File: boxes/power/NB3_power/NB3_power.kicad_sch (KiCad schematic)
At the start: 82 parts, among them J1 Barrel_Jack_PJ-036AH-SMT-TR, J2 Conn_01x02_Male, J3 Conn_01x02_Male, J4 Conn_01x02_Male, J5 Conn_01x04_Male, J6 Conn_01x02_Male, J7 Conn_01x02_Male, Q1 PMOS, Q2 NMOS, SW1 SW_SPDT, U1 NiMH_Charger_LTC4010, U2 Voltage_Regulator_AP64501

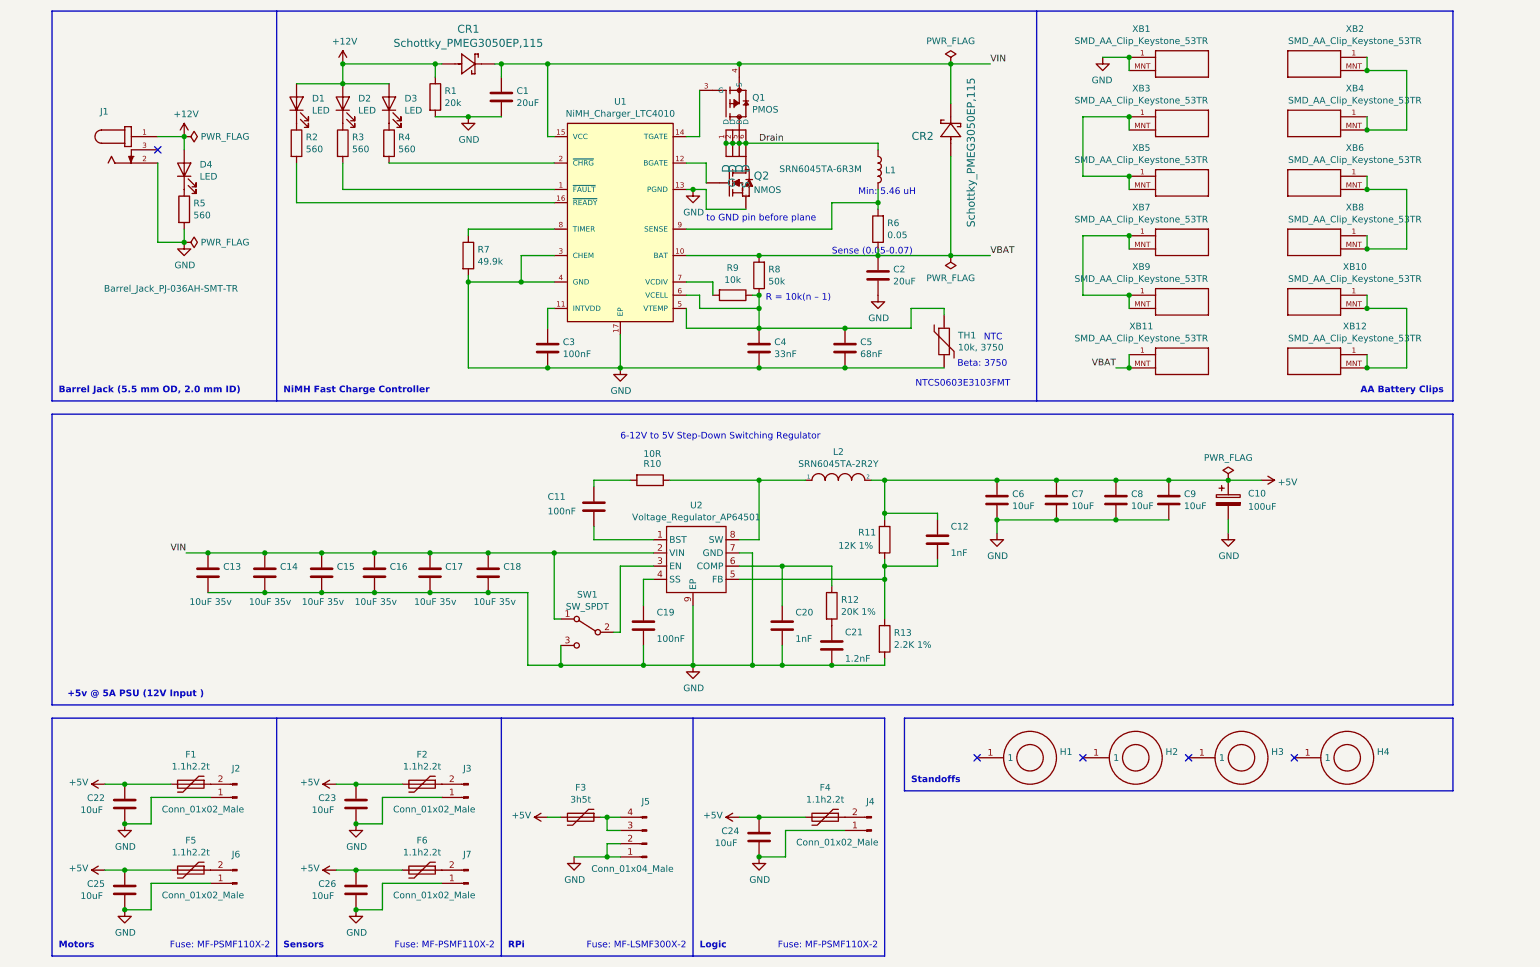
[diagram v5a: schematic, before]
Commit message: NB3_power PCB layout finished
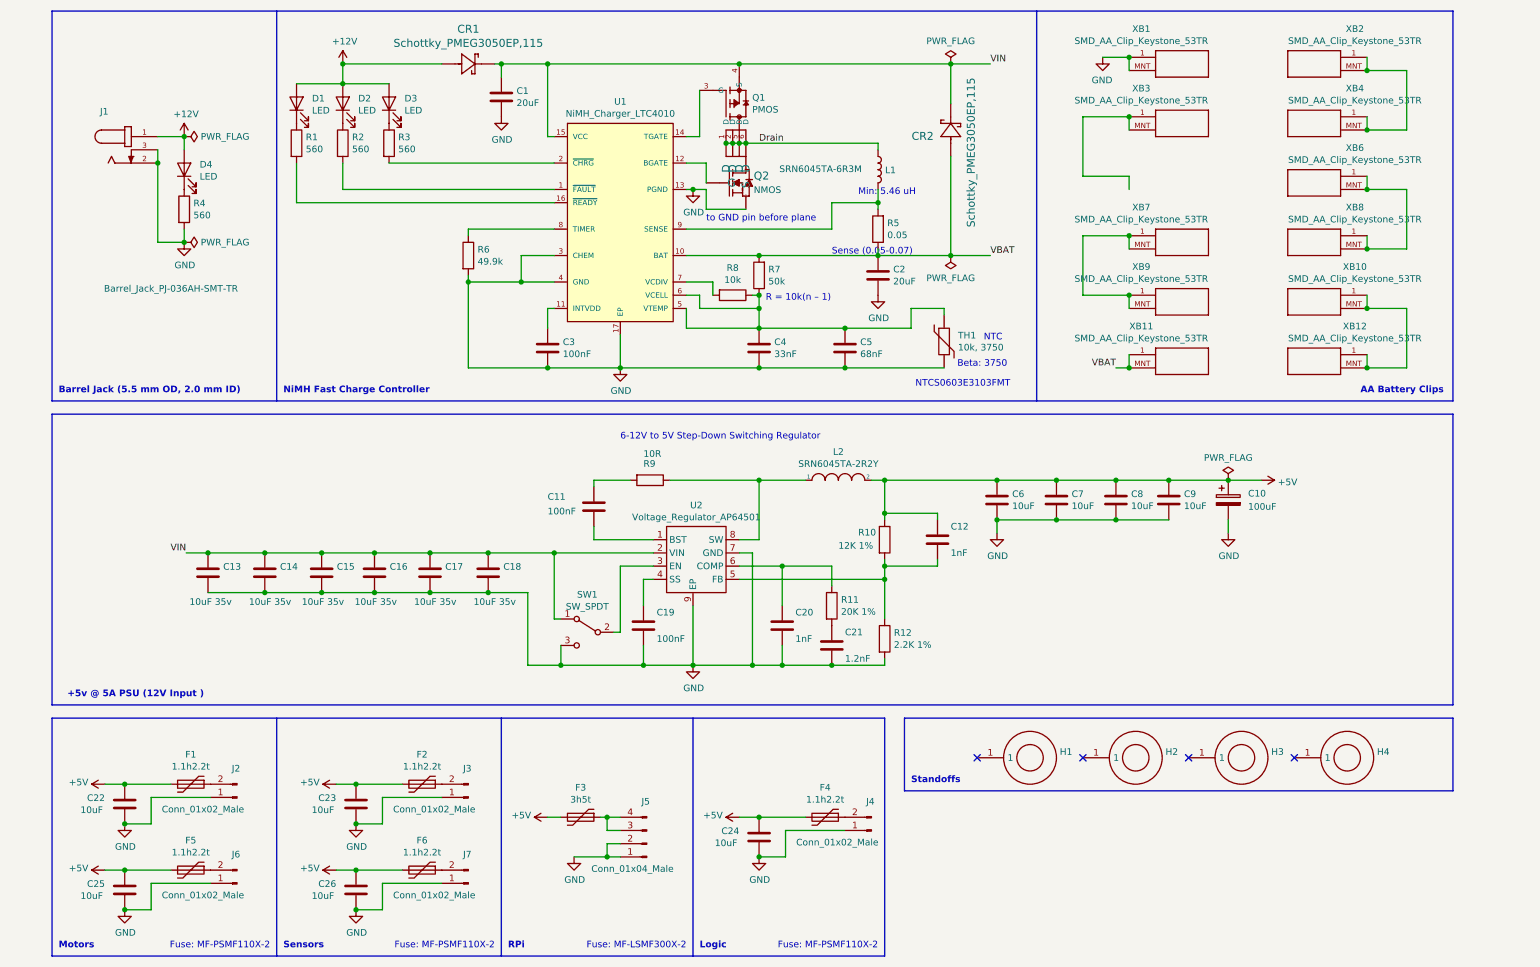
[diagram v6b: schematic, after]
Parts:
- removed R1: 20k, Resistor_SMD:R_0402_1005Metric, symbol Device:R
- removed XB5: SMD_AA_Clip_Keystone_53TR, NB3_power:SMD_AA_Clip_Keystone_53TR, symbol NB3_power:SMD_AA_Clip_Keystone_53TR
- F3: footprint Fuse:Fuse_Bourns_MF-SM_7.98x5.44mm -> Fuse:Fuse_2920_7451Metric
- renumbered R2 to R1, R11 to R10, R12 to R11, R13 to R12, R3 to R2, R4 to R3, R5 to R4, R6 to R5, R7 to R6, R8 to R7, R9 to R8, R10 to R9
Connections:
- net GND: now also J1.3
- no-connect marks 5 -> 4

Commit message: NB3_power PCB fab submisson
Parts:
- C1, C2: value 20uF -> 22uF
- R1, R2, R3, R4: value 560 -> 5.6k
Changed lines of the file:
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@@
   (junction (at 266.7 71.12) (diameter 1.016) (color 0 0 0 0))
   (junction (at 266.7 82.55) (diameter 1.016) (color 0 0 0 0))
-  (no_connect (at 252.73 157.48))
   (no_connect (at 212.09 157.48))
-  (no_connect (at 191.77 157.48))
+  (no_connect (at 252.73 157.48))
   (no_connect (at 232.41 157.48))
+  (no_connect (at 191.77 157.48))
   (wire (pts (xy 24.13 162.56) (xy 27.94 162.56))
     (stroke (width 0) (type solid) (color 0 0 0 0))
@@
       (effects (font (size 1.27 1.27)) (justify left))
     )
-    (property "Value" "560" (id 1) (at 41.148 53.213 0)
+    (property "Value" "5.6k" (id 1) (at 41.148 53.213 0)
       (effects (font (size 1.27 1.27)) (justify left))
     )
@@
       (effects (font (size 1.27 1.27)) (justify left))
     )
-    (property "Value" "560" (id 1) (at 62.738 40.513 0)
+    (property "Value" "5.6k" (id 1) (at 62.738 40.513 0)
       (effects (font (size 1.27 1.27)) (justify left))
     )
@@
       (effects (font (size 1.27 1.27)) (justify left))
     )
-    (property "Value" "560" (id 1) (at 71.628 40.513 0)
+    (property "Value" "5.6k" (id 1) (at 71.628 40.513 0)
       (effects (font (size 1.27 1.27)) (justify left))
     )
@@
       (effects (font (size 1.27 1.27)) (justify left))
     )
-    (property "Value" "560" (id 1) (at 80.518 40.513 0)
+    (property "Value" "5.6k" (id 1) (at 80.518 40.513 0)
       (effects (font (size 1.27 1.27)) (justify left))
     )
@@
       (effects (font (size 1.27 1.27)) (justify left))
     )
-    (property "Value" "20uF" (id 1) (at 103.251 31.623 0)
+    (property "Value" "22uF" (id 1) (at 103.251 31.623 0)
       (effects (font (size 1.27 1.27)) (justify left))
     )
@@
       (effects (font (size 1.27 1.27)) (justify left))
     )
-    (property "Value" "20uF" (id 1) (at 175.641 65.913 0)
+    (property "Value" "22uF" (id 1) (at 175.641 65.913 0)
       (effects (font (size 1.27 1.27)) (justify left))
     )
@@
     )
     (path "/00000000-0000-0000-0000-00005f7de0af"
-      (reference "C1") (unit 1) (value "20uF") (footprint "Capacitor_SMD:C_0805_2012Metric")
+      (reference "C1") (unit 1) (value "22uF") (footprint "Capacitor_SMD:C_0805_2012Metric")
     )
     (path "/00000000-0000-0000-0000-00005f819ed1"
-      (reference "C2") (unit 1) (value "20uF") (footprint "Capacitor_SMD:C_0805_2012Metric")
+      (reference "C2") (unit 1) (value "22uF") (footprint "Capacitor_SMD:C_0805_2012Metric")
     )
     (path "/00000000-0000-0000-0000-00005f80414d"
@@
     )
     (path "/00000000-0000-0000-0000-00005f7ee2db"
-      (reference "R1") (unit 1) (value "560") (footprint "Resistor_SMD:R_0402_1005Metric")
+      (reference "R1") (unit 1) (value "5.6k") (footprint "Resistor_SMD:R_0402_1005Metric")
     )
     (path "/00000000-0000-0000-0000-00005f7eeac0"
-      (reference "R2") (unit 1) (value "560") (footprint "Resistor_SMD:R_0402_1005Metric")
+      (reference "R2") (unit 1) (value "5.6k") (footprint "Resistor_SMD:R_0402_1005Metric")
     )
     (path "/00000000-0000-0000-0000-00005f7ee754"
-      (reference "R3") (unit 1) (value "560") (footprint "Resistor_SMD:R_0402_1005Metric")
+      (reference "R3") (unit 1) (value "5.6k") (footprint "Resistor_SMD:R_0402_1005Metric")
     )
     (path "/00000000-0000-0000-0000-00005f8745a5"
-      (reference "R4") (unit 1) (value "560") (footprint "Resistor_SMD:R_0402_1005Metric")
+      (reference "R4") (unit 1) (value "5.6k") (footprint "Resistor_SMD:R_0402_1005Metric")
     )
     (path "/00000000-0000-0000-0000-00005f83ae1a"

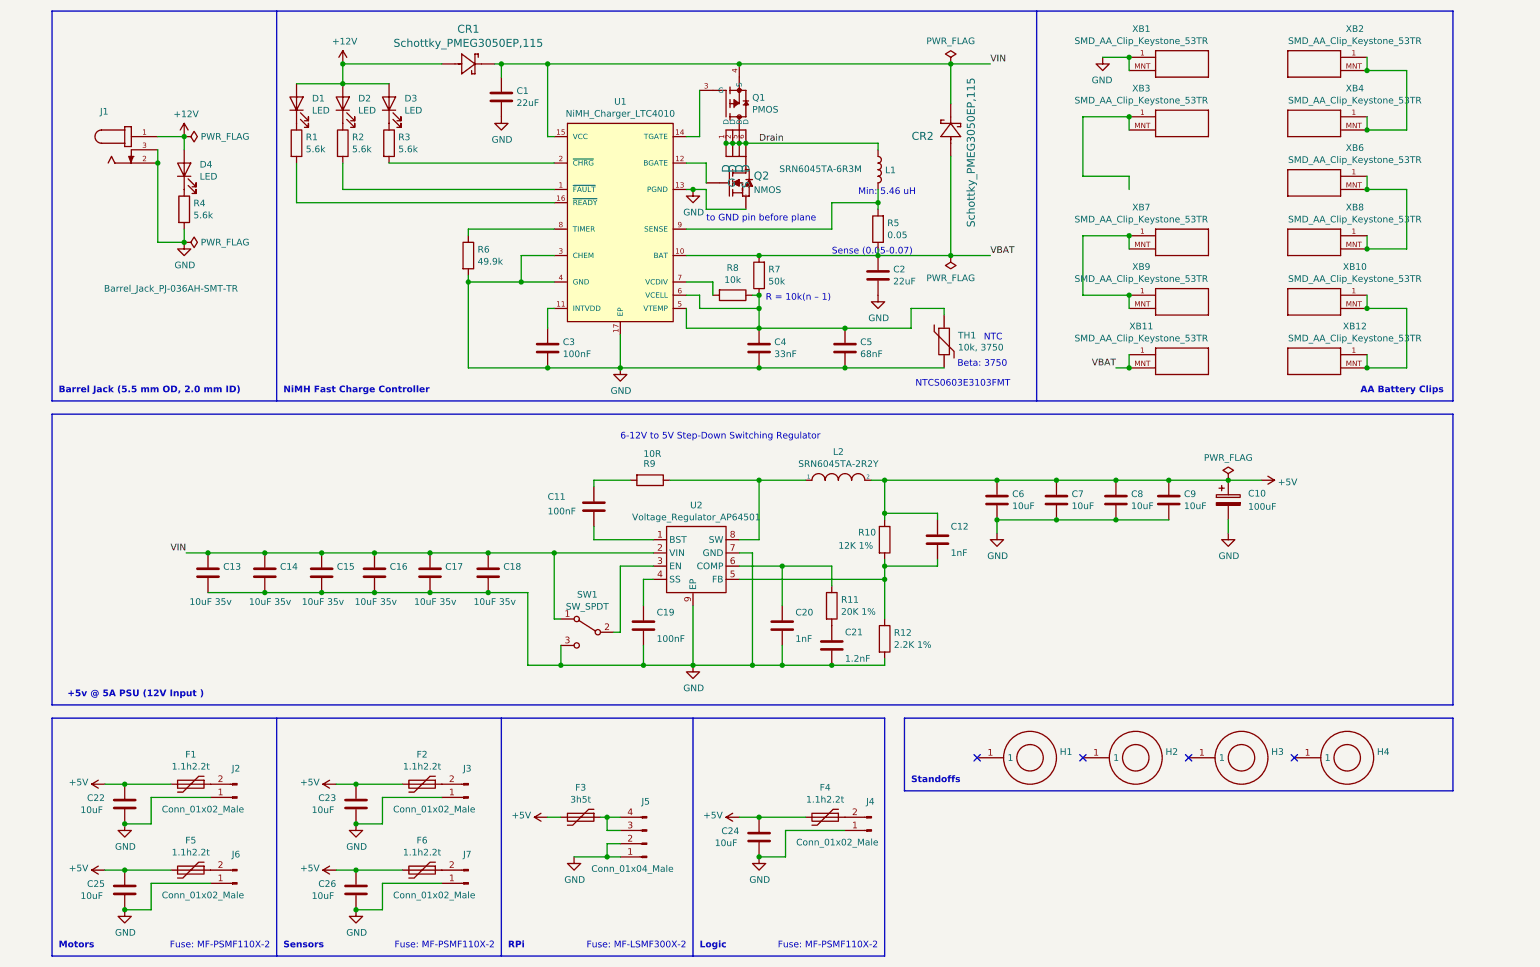
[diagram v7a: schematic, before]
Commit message: Added new NB3 board drafts (body and power)
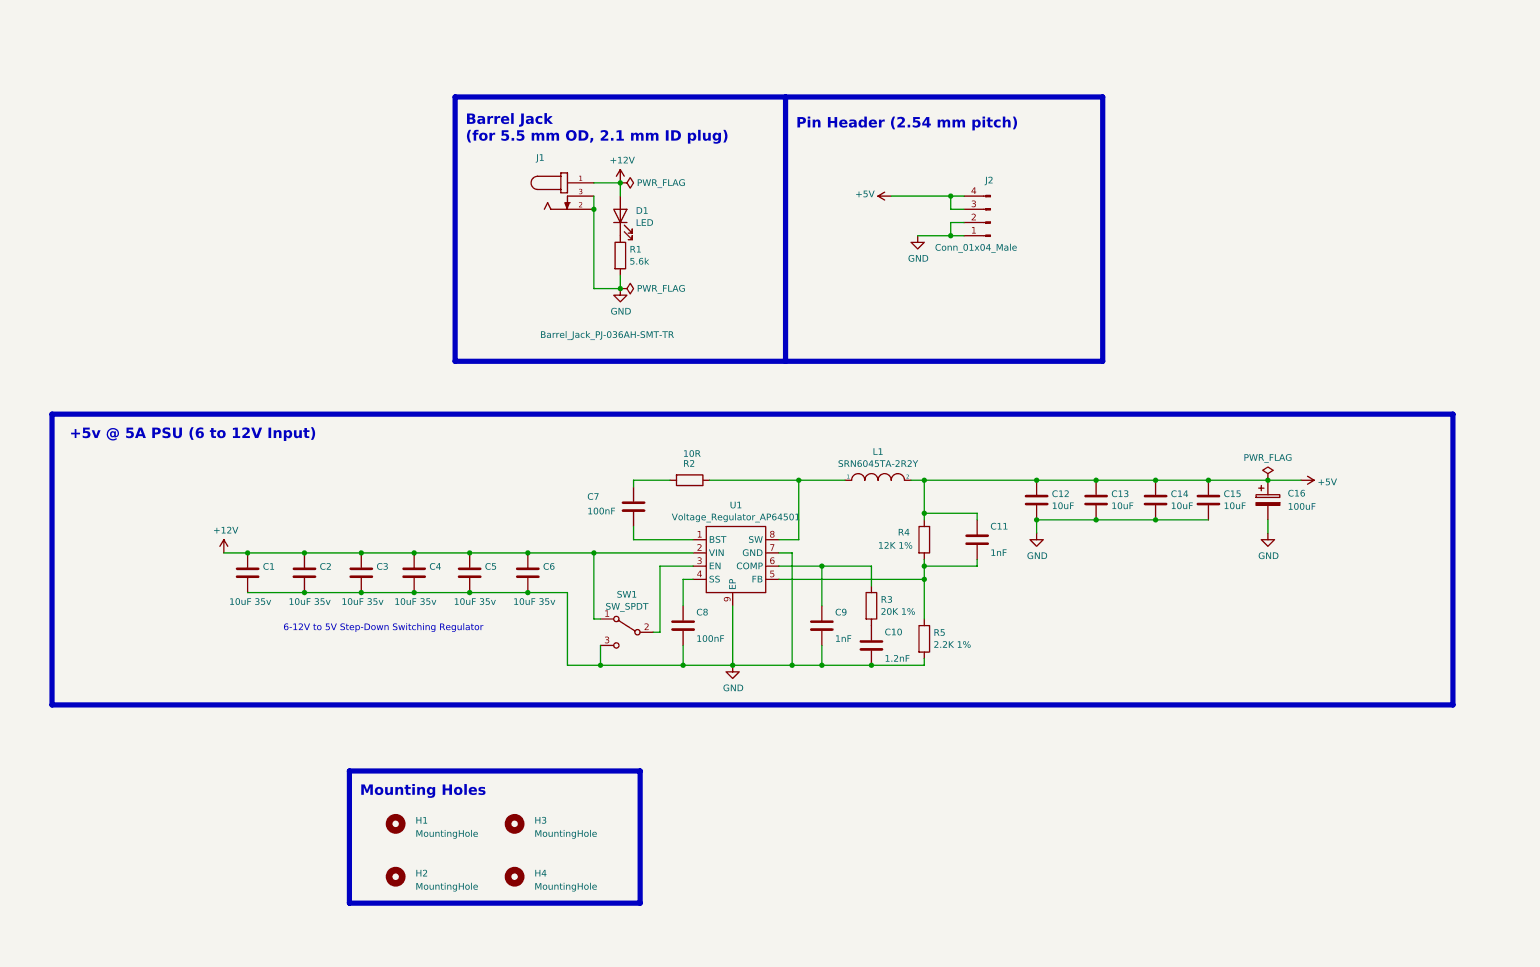
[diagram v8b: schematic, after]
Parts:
- removed C1, C2: 22uF, Capacitor_SMD:C_0805_2012Metric, symbol Device:C
- removed C22, C23, C24, C25, C26: 10uF, Capacitor_SMD:C_0805_2012Metric, symbol Device:C
- removed C3: 100nF, Capacitor_SMD:C_0402_1005Metric, symbol Device:C
- removed C4: 33nF, Capacitor_SMD:C_0402_1005Metric, symbol Device:C
- removed C5: 68nF, Capacitor_SMD:C_0402_1005Metric, symbol Device:C
- removed CR1, CR2: Schottky_PMEG3050EP,115, NB3_power:Schottky_PMEG3050EP,115, symbol NB3_power:Schottky_PMEG3050EP,115
- removed D1, D2, D3: LED, LED_SMD:LED_0603_1608Metric, symbol Device:LED
- removed F1, F2, F4, F5, F6: 1.1h2.2t, Fuse:Fuse_0805_2012Metric, symbol Device:Polyfuse
- removed F3: 3h5t, Fuse:Fuse_2920_7451Metric, symbol Device:Polyfuse
- removed H1, H2, H3, H4: Standoff_SMT_5H_M2.5_9774050151R, NB3_power:Standoff_SMT_5H_M2.5_9774050151R, symbol NB3_power:Standoff_SMT_5H_M2.5_9774050151R
- removed J2, J3, J4, J6, J7: Conn_01x02_Male, Connector_PinHeader_2.54mm:PinHeader_1x02_P2.54mm_Vertical_SMD_Pin1Right, symbol Connector:Conn_01x02_Male
- removed L1: SRN6045TA-6R3M, Inductor_SMD:L_Bourns_SRN6045TA, symbol Device:L
- removed Q1: PMOS, NB3_power:PMOS_SMD_FDC658AP, symbol NB3_power:PMOS_SMD_FDC658AP
- removed Q2: NMOS, NB3_power:NMOS_SMD_SI3410DV-T1-GE3, symbol NB3_power:NMOS_SMD_SI3410DV-T1-GE3
- removed R1, R2, R3: 5.6k, Resistor_SMD:R_0402_1005Metric, symbol Device:R
- removed R5: 0.05, Resistor_SMD:R_1206_3216Metric, symbol Device:R
- removed R6: 49.9k, Resistor_SMD:R_0402_1005Metric, symbol Device:R
- removed R7: 50k, Resistor_SMD:R_0402_1005Metric, symbol Device:R
- removed R8: 10k, Resistor_SMD:R_0402_1005Metric, symbol Device:R
- removed TH1: 10k, 3750, Resistor_SMD:R_0603_1608Metric, symbol Device:Thermistor
- removed U1: NiMH_Charger_LTC4010, NB3_power:NiMH_Charger_LTC4010, symbol NB3_power:NiMH_Charger_LTC4010
- removed XB1, XB10, XB11, XB12, XB2, XB3, XB4, XB6, XB7, XB8, XB9: SMD_AA_Clip_Keystone_53TR, NB3_power:SMD_AA_Clip_Keystone_53TR, symbol NB3_power:SMD_AA_Clip_Keystone_53TR
- added H1, H2, H3, H4: MountingHole, MountingHole:MountingHole_2.7mm_M2.5_ISO7380_Pad, symbol Mechanical:MountingHole
- renumbered C13 to C1, C21 to C10, C12 to C11, C6 to C12, C7 to C13, C8 to C14, C9 to C15, C10 to C16, C14 to C2, C15 to C3, C16 to C4, C17 to C5, C18 to C6, C11 to C7, C19 to C8, C20 to C9, D4 to D1, J5 to J2, L2 to L1, R4 to R1, R9 to R2, R11 to R3, R10 to R4, R12 to R5, U2 to U1
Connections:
- net VIN is gone; now on net +12V: C1.1, C2.1, C3.1, C4.1, C5.1, C6.1, SW1.1 (A), U1.2 (VIN)
- net +5V: now also J2.3 (Pin_3), J2.4 (Pin_4)
- no-connect marks 4 -> 0
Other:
- note added: "+5v @ 5A PSU (6 to 12V Input)"
- note added: "Barrel Jack (for 5.5 mm OD, 2.1 mm ID plug)"
- note added: "Mounting Holes"
- note added: "Pin Header (2.54 mm pitch)"
- note removed: "+5v @ 5A PSU (12V Input )"
- note removed: "AA Battery Clips"
- note removed: "Barrel Jack (5.5 mm OD, 2.0 mm ID)"
- note removed: "Beta: 3750"
- note removed: "Fuse: MF-LSMF300X-2"
- note removed: "Fuse: MF-PSMF110X-2"
- note removed: "Logic"
- note removed: "Min: 5.46 uH"
- note removed: "Motors"
- note removed: "NTC"
- note removed: "NTCS0603E3103FMT"
- note removed: "NiMH Fast Charge Controller"
- note removed: "R = 10k(n – 1)"
- note removed: "RPi"
- note removed: "Sense (0.05-0.07)"
- note removed: "Sensors"
- note removed: "Standoffs"
- note removed: "to GND pin before plane"
- moved on the sheet: C1, C10, C11, C12, C13, C14, C15, C16, C2, C3, C4, C5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
